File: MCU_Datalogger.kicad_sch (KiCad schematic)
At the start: 24 parts, among them U1 ATMEGA328P-AU, U2 DS1337S_, U3 24LC1025, U4 24LC1025, Y1 Crystal, Y2 Crystal

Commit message: Schematic Complete
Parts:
- removed D1, D2: D, symbol Device:D
- added BT1: Battery, Connector_PinHeader_2.54mm:PinHeader_1x02_P2.54mm_Vertical, symbol Device:Battery
- added D1, D2: LED, symbol Device:LED
- C1, C4: value C -> 0.1uF; footprint (none) -> Capacitor_SMD:C_0805_2012Metric
- C2, C3: value C -> 22pF; footprint (none) -> Capacitor_SMD:C_0805_2012Metric
- C5: value C -> 100nF; footprint (none) -> Capacitor_SMD:C_0805_2012Metric
- H1, H2, H3, H4: footprint (none) -> MountingHole:MountingHole_2.1mm
- R1, R2, R6: value R_US -> 10K; footprint (none) -> Resistor_SMD:R_0805_2012Metric
- R3, R4: value R_US -> 4.7K; footprint (none) -> Resistor_SMD:R_0805_2012Metric
- R5, R7: value R_US -> 330; footprint (none) -> Resistor_SMD:R_0805_2012Metric
- U3, U4: footprint (none) -> Package_SO:SOIC-8_5.3x5.3mm_P1.27mm
- Y1: value Crystal -> 32.768 KHz; footprint (none) -> Crystal:Crystal_SMD_5032-2Pin_5.0x3.2mm_HandSoldering
- Y2: value Crystal -> 16 MHz; footprint (none) -> Crystal:Crystal_SMD_5032-2Pin_5.0x3.2mm_HandSoldering
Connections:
- net at R7.1: now also D2.1 (K)
- net GND: now reaches R7.2
- net GND: now also C1.2, C2.1, C3.1, C4.2, C5.2, R5.1, U1.21 (GND), U1.3 (GND), U1.5 (GND), U2.4 (GND), U3.4 (GND), U3.7 (WP), U4.2 (A1), U4.4 (GND), U4.7 (WP), BT1.2 (-)
- net at C4.1: now also U1.20 (AREF)
- net at C5.1: now also U1.18 (AVCC), U1.4 (VCC), BT1.1 (+), D2.2 (A)
- net Vcc: now reaches R4.1
- net Vcc: now also C1.1, R1.1, R2.1, R3.1, R6.1, U2.8 (VCC), U3.1 (A0), U3.2 (A1), U3.3 (A2), U3.8 (VCC), U4.1 (A0), U4.3 (A2), U4.8 (VCC)
- net SDA: now reaches R4.2
- net SDA: now also U1.27 (PC4), U2.5 (SDA), U3.5 (SDA), U4.5 (SDA)
- net at R2.2: now also U2.7 (SQW/~INT)
- net at R5.2: now also D1.1 (K)
- net RESET: now reaches R6.2
- net RESET: now also U1.29 (PC6)
- net D3: now reaches U1.1 (PD3)
- net D6: now reaches U1.10 (PD6)
- net D7: now reaches U1.11 (PD7)
- net D8: now reaches U1.12 (PB0)
- net MOSI: now reaches U1.15 (PB3)
- net MISO: now reaches U1.16 (PB4)
- net SCK: now reaches U1.17 (PB5)
- net SCK: now also D1.2 (A)
- net D4: now reaches U1.2 (PD4)
- net SCL: now reaches U1.28 (PC5)
- net SCL: now also R3.2, U2.6 (SCL), U3.6 (SCL), U4.6 (SCL)
- net RX: now reaches U1.30 (PD0)
- net TX: now reaches U1.31 (PD1)
- net D2: now reaches U1.32 (PD2)
- net at U1.7 (PB6): now also C2.2, Y2.2
- net at U1.8 (PB7): now also C3.2, Y2.1
- net D5: now reaches U1.9 (PD5)
- net at R1.2: now also U2.3 (~{INTA})
- net at U2.1 (X1): now also Y1.2
- net at U2.2 (X2): now also Y1.1
- no-connect marks 0 -> 9
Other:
- sheet Connectors ports: added D2, D3, D4, D5, D6, D7, D8, GND, MISO, MOSI, RESET, RX, SCK, SCL, SDA, TX, Vcc; removed none
- moved on the sheet: C1, C2, C3, C4, C5, H1, H2, H3, H4, R1, R2, R3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

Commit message: Schematic ok
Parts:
- D1, D2: footprint (none) -> LED_SMD:LED_0805_2012Metric
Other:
- note added: "EEPROM"
- note added: "MCU"
- note added: "Mounting Holes"
- note added: "Real-Time clock"
- moved on the sheet: BT1, C2, C3, C4, C5, D1, D2, H1, H2, H3, H4, R5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

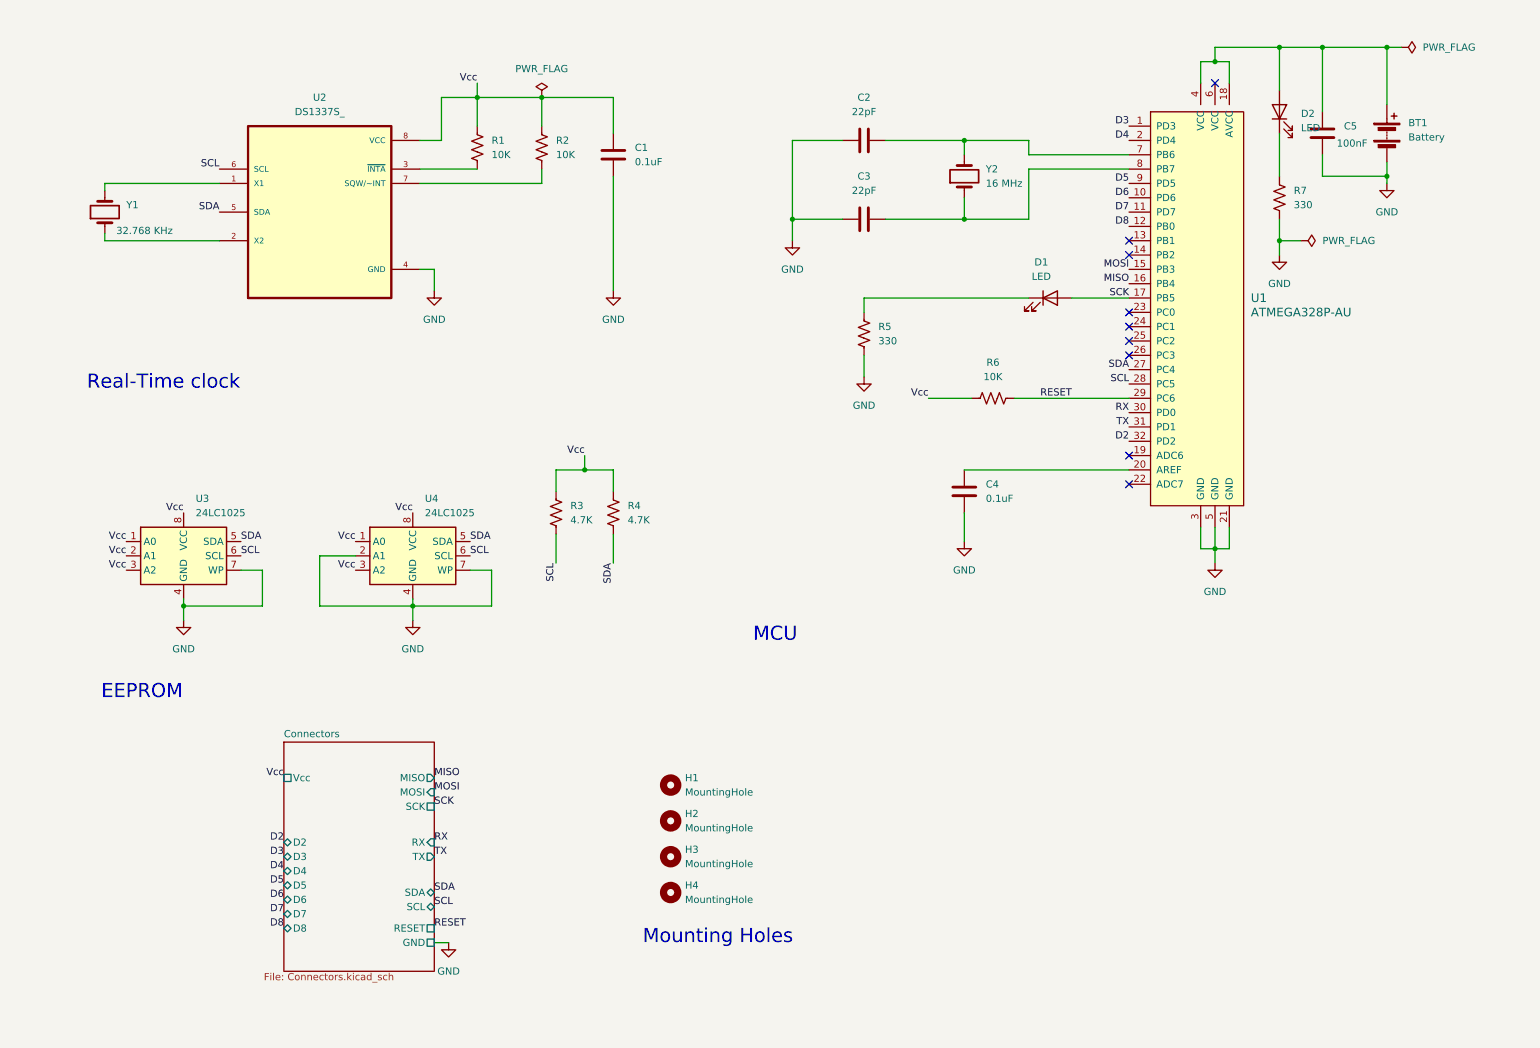
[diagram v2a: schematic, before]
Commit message: Restore Schematic from 2layer
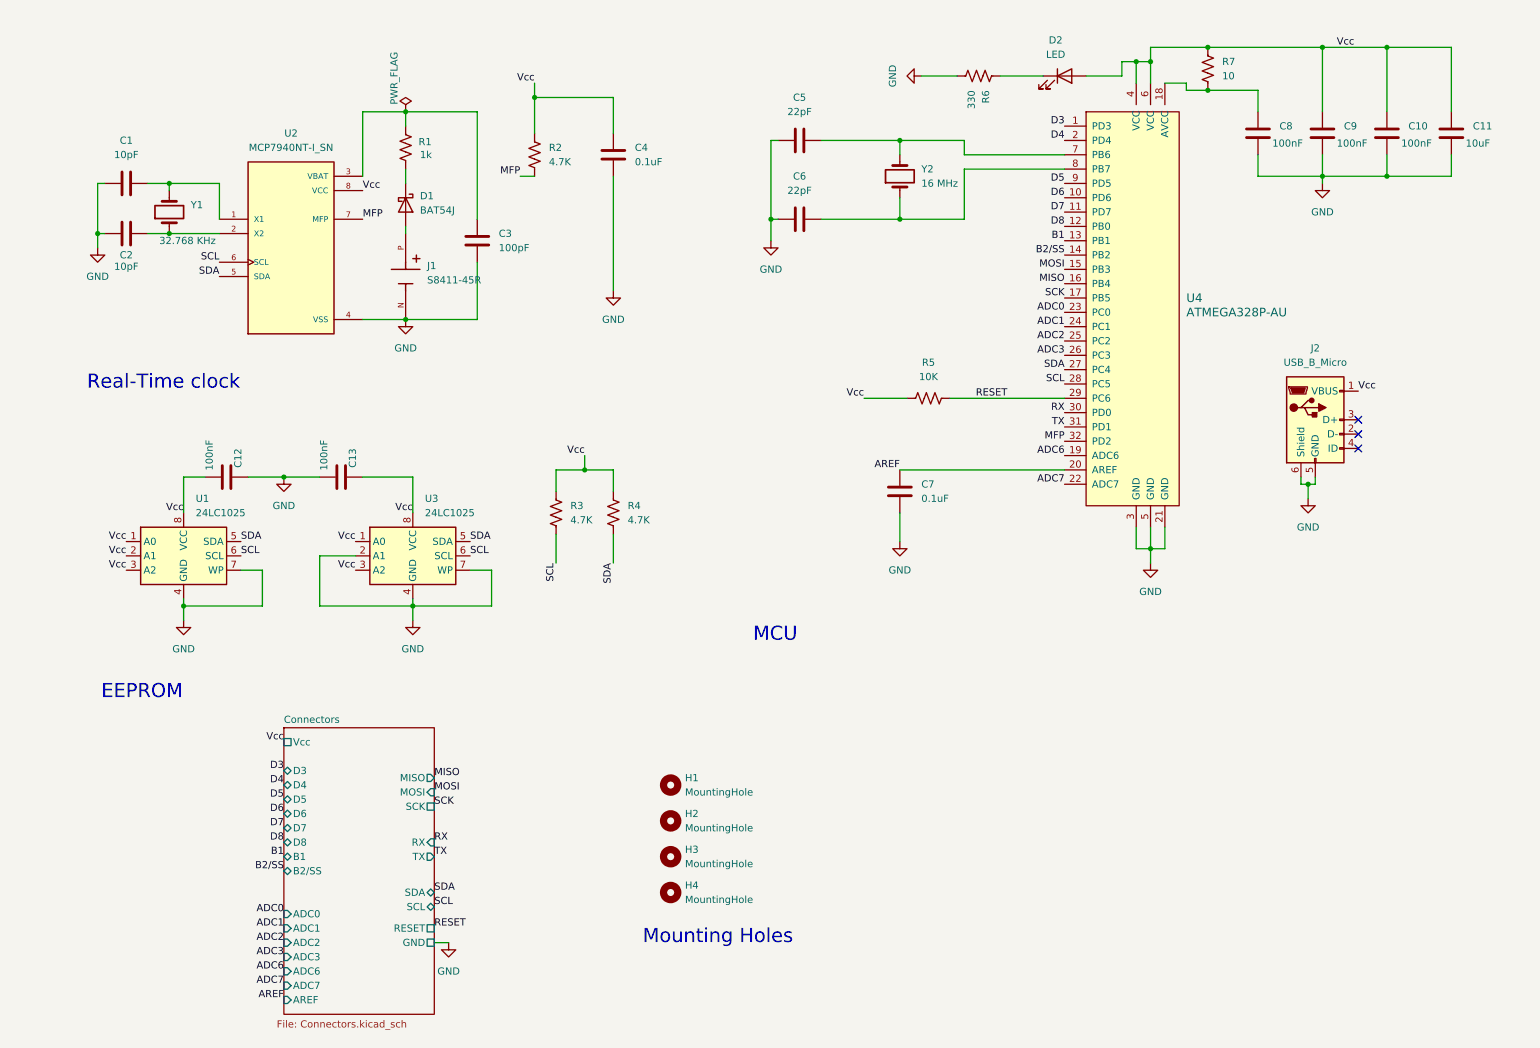
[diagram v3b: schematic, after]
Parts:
- removed BT1: Battery, Connector_PinHeader_2.54mm:PinHeader_1x02_P2.54mm_Vertical, symbol Device:Battery
- removed D1: LED, LED_SMD:LED_0805_2012Metric, symbol Device:LED
- removed R2: 10K, Resistor_SMD:R_0805_2012Metric, symbol Device:R_US
- removed R5: 330, Resistor_SMD:R_0805_2012Metric, symbol Device:R_US
- removed U2: DS1337S_, DS1337S_:SOIC127P600X175-8N, symbol DS1337S_:DS1337S_
- added C1, C2: 10pF, Capacitor_SMD:C_0805_2012Metric, symbol Device:C
- added C10, C12, C13, C9: 100nF, Capacitor_SMD:C_0805_2012Metric, symbol Device:C
- added C11: 10uF, Capacitor_SMD:C_0805_2012Metric, symbol Device:C
- added C3: 100pF, Capacitor_SMD:C_0805_2012Metric, symbol Device:C
- added D1: BAT54J, Diode_SMD:D_SOD-323F, symbol Diode:BAT54J
- added J1: S8411-45R, S8411-45R:HARWIN_S8411-45R, symbol S8411-45R:S8411-45R
- added J2: USB_B_Micro, digikey-footprints:USB_Micro_B_Female_6pin, symbol Connector:USB_B_Micro
- added R1: 1k, Resistor_SMD:R_0805_2012Metric, symbol Device:R_US
- added R7: 10, Resistor_SMD:R_0805_2012Metric, symbol Device:R_US
- added U2: MCP7940NT-I_SN, MCP7940N_SOIC:SOIC127P600X175-8N, symbol MCP7940NT-I_SN:MCP7940NT-I_SN
- R2: renamed from R1; value 10K -> 4.7K
- Y1: footprint Crystal:Crystal_SMD_5032-2Pin_5.0x3.2mm_HandSoldering -> FC-135_32.7680KA-A0:XTAL_FC-135_32.7680KA-A0
- renumbered C1 to C4, C2 to C5, C3 to C6, C4 to C7, C5 to C8, R6 to R5, R7 to R6, U3 to U1, U4 to U3, U1 to U4
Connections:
- net D2 is gone; now on net MFP: U4.32 (PD2)
- net GND: now also C1.1, C10.2, C11.2, C12.1, C13.2, C2.1, C3.2, C9.2, J1.N, J2.5 (GND), J2.6 (Shield), U2.4 (VSS)
- net SCL: now also U2.6 (SCL)
- net SDA: now also U2.5 (SDA)
- net Vcc: now also D2.2 (A), U4.4 (VCC), U4.6 (VCC), C10.1, C11.1, C12.2, C13.1, C9.1, J2.1 (VBUS), R7.2, U2.8 (VCC)
- net AREF: now reaches C7.1, U4.20 (AREF)
- net at C8.1, U4.18 (AVCC): now also R7.1; no longer D2.2 (A), U4.4 (VCC)
- net B1: now reaches U4.13 (PB1)
- net B2/SS: now reaches U4.14 (PB2)
- net ADC6: now reaches U4.19 (ADC6)
- net ADC7: now reaches U4.22 (ADC7)
- net ADC0: now reaches U4.23 (PC0)
- net ADC1: now reaches U4.24 (PC1)
- net ADC2: now reaches U4.25 (PC2)
- net ADC3: now reaches U4.26 (PC3)
- net MFP: now reaches R2.2
- net MFP: now also U2.7 (MFP)
- net at Y1.2: now also C1.2, U2.1 (X1)
- net at Y1.1: now also C2.2, U2.2 (X2)
- new net: D1.1 (K), R1.2
- new net: D1.2 (A), J1.P
- new net: C3.1, R1.1, U2.3 (VBAT)
- no-connect marks 9 -> 3
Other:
- sheet Connectors ports: added ADC0, ADC1, ADC2, ADC3, ADC6, ADC7, AREF, B1, B2/SS; removed D2
- moved on the sheet: C5, C6, C7, C8, D2, R2, R5, R6, U4, Y1, Y2
